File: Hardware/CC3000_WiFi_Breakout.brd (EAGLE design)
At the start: 40.6 x 35.6 mm, 33 parts, among them J1 U.FL, U1 V_REG_317SMD, U3 74HC4050, U5 CC3000

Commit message: Layout (mostly) done
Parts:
- U1: value V_REG_317SMD -> (none)
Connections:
- net 3.3V: now also U1.4
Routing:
- net 3.3V: track 101.9 -> 89.4 mm, vias 3 -> 13
- net VCC: track 45.2 -> 47.9 mm
- net D3: track 18.2 -> 16.6 mm
- added copper zone on layer 1, net 3.3V
- added copper zone on layer 16, net 3.3V

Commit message: Proto layout complete. Needs aesthetics.
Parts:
- moved LOGO2 48.2 mm to (27.7, 8.64), turned to 0 degrees
- moved AE1 30.7 mm to (10.2, 38.1), turned to 180 degrees
- moved J1 30.5 mm to (27.9, 36.8), turned to 270 degrees
- moved STANDOFF1 30.5 mm to (33.0, 33.0), turned to 90 degrees
- moved STANDOFF2 30.5 mm to (2.54, 33.0), turned to 90 degrees
- moved STANDOFF3 30.5 mm to (2.54, 2.54), turned to 90 degrees
- moved STANDOFF4 30.5 mm to (33.0, 2.54), turned to 90 degrees
- moved C7 28.7 mm to (17.8, 38.1), turned to 0 degrees
- moved L2 27.7 mm to (20.1, 37.2), turned to 270 degrees
- moved L1 27.7 mm to (15.5, 37.2), turned to 270 degrees
- moved JP2 27.1 mm to (27.9, 2.54), turned to 180 degrees
- moved C5 24.4 mm to (31.8, 7.62), turned to 180 degrees
- moved D1 21.7 mm to (3.81, 11.4), turned to 270 degrees
- moved C6 20.9 mm to (23.7, 31.3), turned to 270 degrees
- moved C1 20.5 mm to (8.89, 29.2), turned to 0 degrees
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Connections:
- net D4 renamed INT
- net D5 renamed CS
- removed net D1: JP2.1, U3.3
- removed net D2: JP2.2, U3.5
- removed net D3: JP2.3, U3.7
- new net EN: JP2.2, U3.3
- new net MOSI: JP2.7, U3.7
- new net SCK: JP2.3, U3.5
- net GND: now also JP2.1; no longer JP2.7
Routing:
- net D1: track 30.5 -> 0.00 mm, vias 2 -> 0
- net EN: track 0.00 -> 30.3 mm, vias 0 -> 2
- net D2: track 27.1 -> 0.00 mm, vias 1 -> 0
- net SCK: track 0.00 -> 23.4 mm, vias 0 -> 1
- net D3: track 16.6 -> 0.00 mm, vias 1 -> 0
- net MOSI: track 0.00 -> 6.95 mm
- net INT: track 10.0 -> 7.41 mm
- net VCC: track 47.9 -> 45.7 mm
- net CS: track 12.1 -> 10.1 mm
- net WIFI_EN: track 47.0 -> 48.7 mm
- net SPI_MISO: track 19.3 -> 18.0 mm
- net 3.3V: track 89.4 -> 88.4 mm
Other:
- board size 40.6 x 35.6 mm -> 35.6 x 40.6 mm

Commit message: Prototype board ready for review
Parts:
- U1: value (none) -> LM1117
- moved LOGO3 69.0 mm to (3.17, 26.7)
- moved LOGO1 61.2 mm to (3.81, 7.62)
- moved FID2 58.5 mm to (1.27, 6.35)
- moved FID1 38.6 mm to (34.3, 29.2)
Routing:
- net 3.3V: track 88.4 -> 88.9 mm
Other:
- board text added: "3.3V"
- board text added: "CS"
- board text added: "EN"
- board text added: "INT"
- board text added: "MISO"
- board text added: "MOSI"
- board text added: "SCK"
- board text added: "VCC"
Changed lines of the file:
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@@
 <setting verticaltext="up"/>
 </settings>
-<grid distance="0.05" unitdist="inch" unit="inch" style="dots" multiple="1" display="yes" altdistance="0.025" altunitdist="inch" altunit="inch"/>
+<grid distance="0.05" unitdist="inch" unit="inch" style="dots" multiple="1" display="yes" altdistance="0.005" altunitdist="inch" altunit="inch"/>
 <layers>
 <layer number="1" name="Top" color="4" fill="1" visible="yes" active="yes"/>
-<layer number="16" name="Bottom" color="1" fill="1" visible="no" active="yes"/>
+<layer number="16" name="Bottom" color="1" fill="1" visible="yes" active="yes"/>
 <layer number="17" name="Pads" color="2" fill="1" visible="yes" active="yes"/>
 <layer number="18" name="Vias" color="2" fill="1" visible="yes" active="yes"/>
@@
 <layer number="20" name="Dimension" color="15" fill="1" visible="yes" active="yes"/>
 <layer number="21" name="tPlace" color="16" fill="1" visible="yes" active="yes"/>
-<layer number="22" name="bPlace" color="14" fill="1" visible="no" active="yes"/>
+<layer number="22" name="bPlace" color="14" fill="1" visible="yes" active="yes"/>
 <layer number="23" name="tOrigins" color="15" fill="1" visible="yes" active="yes"/>
-<layer number="24" name="bOrigins" color="15" fill="1" visible="no" active="yes"/>
+<layer number="24" name="bOrigins" color="15" fill="1" visible="yes" active="yes"/>
 <layer number="25" name="tNames" color="7" fill="1" visible="no" active="yes"/>
 <layer number="26" name="bNames" color="7" fill="1" visible="no" active="yes"/>
@@
 <layer number="43" name="vRestrict" color="2" fill="10" visible="no" active="yes"/>
 <layer number="44" name="Drills" color="7" fill="1" visible="no" active="yes"/>
-<layer number="45" name="Holes" color="7" fill="1" visible="no" active="yes"/>
+<layer number="45" name="Holes" color="7" fill="1" visible="yes" active="yes"/>
 <layer number="46" name="Milling" color="3" fill="1" visible="no" active="yes"/>
-<layer number="51" name="tDocu" color="6" fill="1" visible="no" active="yes"/>
+<layer number="51" name="tDocu" color="6" fill="1" visible="yes" active="yes"/>
 <layer number="52" name="bDocu" color="7" fill="1" visible="no" active="yes"/>
 <layer number="33" name="tFinish" color="6" fill="3" visible="no" active="no"/>
@@
 <text x="15.875" y="24.13" size="0.8128" layer="21" font="vector" ratio="15" rot="R90" align="center">RX</text>
 <text x="15.875" y="26.67" size="0.8128" layer="21" font="vector" ratio="15" rot="R270" align="center">TX</text>
-<text x="95.25" y="3.175" size="1.016" layer="21" font="vector" ratio="15" rot="R270" align="center">Debug</text>
+<text x="17.78" y="28.575" size="0.8128" layer="21" font="vector" ratio="15" rot="R180" align="center">Debug</text>
 <text x="31.75" y="-16.51" size="1.778" layer="25" font="vector">Shawn Hymel</text>
 <text x="34.29" y="20.32" size="1.2192" layer="16" font="vector" ratio="15" rot="MR270" align="center">v01</text>
-<text x="85.09" y="10.16" size="1.397" layer="21" font="vector" ratio="15" rot="R180" align="bottom-center">CC3000</text>
-<text x="85.09" y="15.24" size="1.397" layer="21" font="vector" ratio="15" align="bottom-center">WiFi Breakout</text>
-<text x="74.93" y="30.48" size="1.016" layer="21" font="vector" ratio="15" align="bottom-center">802.11b/g</text>
-<text x="76.2" y="2.54" size="1.016" layer="21" font="vector" ratio="15" rot="R90" align="bottom-center">PWR</text>
+<text x="15.24" y="32.0548" size="1.27" layer="21" font="vector" ratio="15" align="bottom-center">CC3000</text>
+<text x="15.24" y="30.5816" size="1.27" layer="21" font="vector" ratio="15" align="bottom-center">WiFi Breakout</text>
+<text x="26.67" y="9.144" size="1.016" layer="21" font="vector" ratio="15" align="bottom-center">802.11b/g</text>
+<text x="1.27" y="11.43" size="0.8128" layer="21" font="vector" ratio="15" rot="R270" align="bottom-center">PWR</text>
 <wire x1="0" y1="40.64" x2="0" y2="0" width="0.2032" layer="20"/>
 <wire x1="0" y1="0" x2="35.56" y2="0" width="0.2032" layer="20"/>
@@
 <vertex x="0" y="37.846"/>
 </polygon>
+<text x="27.94" y="0.7112" size="0.8128" layer="21" font="vector" ratio="15" align="center">GND</text>
+<text x="25.4" y="4.3688" size="0.8128" layer="21" font="vector" ratio="15" align="center">EN</text>
+<text x="22.86" y="0.7112" size="0.8128" layer="21" font="vector" ratio="15" align="center">SCK</text>
+<text x="20.32" y="4.3688" size="0.8128" layer="21" font="vector" ratio="15" align="center">INT</text>
+<text x="17.78" y="0.7112" size="0.8128" layer="21" font="vector" ratio="15" align="center">CS</text>
+<text x="15.24" y="4.3688" size="0.8128" layer="21" font="vector" ratio="15" align="center">MISO</text>
+<text x="12.7" y="0.7112" size="0.8128" layer="21" font="vector" ratio="15" align="center">MOSI</text>
+<text x="10.16" y="4.3688" size="0.8128" layer="21" font="vector" ratio="15" align="center">3.3V</text>
+<text x="7.62" y="0.7112" size="0.8128" layer="21" font="vector" ratio="15" align="center">VCC</text>
 </plain>
 <attributes>
@@
 <param name="dpGapFactor" value="2.5"/>
 <param name="checkGrid" value="0"/>
-<param name="checkAngle" value="1"/>
+<param name="checkAngle" value="0"/>
 <param name="checkFont" value="1"/>
 <param name="checkRestrict" value="1"/>
@@
 <element name="R1" library="SparkFun-Resistors" package="0603-RES" value="240" x="8.89" y="17.78" rot="R180"/>
 <element name="R2" library="SparkFun-Resistors" package="0603-RES" value="390" x="13.97" y="17.78" rot="R180"/>
-<element name="U1" library="SparkFun-PowerIC" package="SOT223" value="" x="6.35" y="22.86" rot="R90"/>
+<element name="U1" library="SparkFun-PowerIC" package="SOT223" value="LM1117" x="6.35" y="22.86" rot="R90"/>
 <element name="U3" library="SparkFun-DigitalIC" package="SO016" value="74HC4050" x="11.43" y="10.16" rot="R270"/>
 <element name="SJ1" library="SparkFun-Passives" package="SJ_3_PASTE1&amp;2" value="Mode" x="17.78" y="11.43" rot="R180"/>
@@
 </element>
 <element name="R4" library="SparkFun-Resistors" package="0603-RES" value="10k" x="3.81" y="17.78" rot="R180"/>
-<element name="FID1" library="SparkFun-Aesthetics" package="FIDUCIAL-1X2" value="FIDUCIAL1X2" x="62.23" y="2.54"/>
-<element name="FID2" library="SparkFun-Aesthetics" package="FIDUCIAL-1X2" value="FIDUCIAL1X2" x="59.69" y="2.54"/>
-<element name="LOGO1" library="SparkFun-Aesthetics" package="OSHW-LOGO-S" value="OSHW-LOGOS" x="64.77" y="2.54"/>
+<element name="FID1" library="SparkFun-Aesthetics" package="FIDUCIAL-1X2" value="FIDUCIAL1X2" x="34.29" y="29.21"/>
+<element name="FID2" library="SparkFun-Aesthetics" package="FIDUCIAL-1X2" value="FIDUCIAL1X2" x="1.27" y="6.35"/>
+<element name="LOGO1" library="SparkFun-Aesthetics" package="OSHW-LOGO-S" value="OSHW-LOGOS" x="3.81" y="7.62"/>
 <element name="LOGO2" library="SparkFun-Aesthetics" package="SFE-NEW-WEBLOGO" value="LOGO-SFENEW" x="27.686" y="8.636" rot="MR0"/>
-<element name="LOGO3" library="SparkFun-Aesthetics" package="SFE-LOGO-FLAME" value="LOGO-SFESK" x="67.31" y="1.27"/>
+<element name="LOGO3" library="SparkFun-Aesthetics" package="SFE-LOGO-FLAME" value="LOGO-SFESK" x="3.175" y="26.67"/>
 <element name="JP2" library="SparkFun-Connectors" package="1X09" value="M09" x="27.94" y="2.54" rot="R180"/>
 <element name="STANDOFF1" library="SparkFun-Electromechanical" package="STAND-OFF" value="STAND-OFF" x="33.02" y="33.02" rot="R90"/>
@@
 <wire x1="2.96" y1="17.78" x2="2.96" y2="17.106" width="0.254" layer="1"/>
 <wire x1="2.96" y1="17.106" x2="3.81" y2="16.256" width="0.254" layer="1"/>
-<wire x1="3.81" y1="16.256" x2="5.334" y2="16.256" width="0.254" layer="1"/>
-<wire x1="5.334" y1="16.256" x2="6.731" y2="14.859" width="0.254" layer="1"/>
-<wire x1="6.731" y1="14.859" x2="6.985" y2="14.605" width="0.254" layer="1"/>
-<wire x1="8.63" y1="14.605" x2="6.985" y2="14.605" width="0.254" layer="1"/>
-<wire x1="4.66" y1="13.97" x2="5.842" y2="13.97" width="0.254" layer="1"/>
-<wire x1="5.842" y1="13.97" x2="6.731" y2="14.859" width="0.254" layer="1"/>
+<wire x1="3.81" y1="16.256" x2="5.842" y2="16.256" width="0.254" layer="1"/>
+<wire x1="4.66" y1="13.97" x2="6.35" y2="13.97" width="0.254" layer="1"/>
 <contactref element="U1" pad="4"/>
 <polygon width="0.254" layer="1" isolate="0.3048">
@@
 <wire x1="29.464" y1="8.128" x2="27.178" y2="10.414" width="0.508" layer="16"/>
 <wire x1="27.178" y1="10.414" x2="21.336" y2="10.414" width="0.508" layer="16"/>
-</signal>
-<signal name="GND" airwireshidden="yes">
+<wire x1="8.63" y1="14.605" x2="7.493" y2="14.605" width="0.254" layer="1"/>
+<wire x1="7.493" y1="14.605" x2="7.239" y2="14.859" width="0.254" layer="1"/>
+<wire x1="7.239" y1="14.859" x2="5.842" y2="16.256" width="0.254" layer="1"/>
+<wire x1="6.35" y1="13.97" x2="7.239" y2="14.859" width="0.254" layer="1"/>
+</signal>
+<signal name="GND">
 <contactref element="C1" pad="C"/>
 <contactref element="C3" pad="2"/>
@@
 <via x="20.828" y="27.94" extent="1-16" drill="0.381"/>
 <via x="19.431" y="14.859" extent="1-16" drill="0.381"/>
+<via x="13.97" y="15.748" extent="1-16" drill="0.508"/>
+<via x="1.016" y="28.956" extent="1-16" drill="0.508"/>
+<via x="16.51" y="29.845" extent="1-16" drill="0.508"/>
+<via x="5.1308" y="15.2908" extent="1-16" drill="0.508"/>
+<via x="5.842" y="1.016" extent="1-16" drill="0.508"/>
+<via x="29.718" y="1.016" extent="1-16" drill="0.508"/>
+<via x="34.036" y="6.096" extent="1-16" drill="0.508"/>
+<via x="11.43" y="8.128" extent="1-16" drill="0.508"/>
+<via x="6.604" y="32.004" extent="1-16" drill="0.508"/>
+<via x="23.876" y="4.572" extent="1-16" drill="0.508"/>
+<via x="21.844" y="4.572" extent="1-16" drill="0.508"/>
+<via x="34.29" y="39.37" extent="1-16" drill="0.508"/>
 </signal>
 <signal name="WIFI_CS">
@@
 <wire x1="15.748" y1="4.572" x2="13.462" y2="4.572" width="0.254" layer="1"/>
 </signal>
+<signal name="N$1">
+<via x="16.002" y="25.4" extent="1-16" drill="0.508"/>
+</signal>
 </signals>

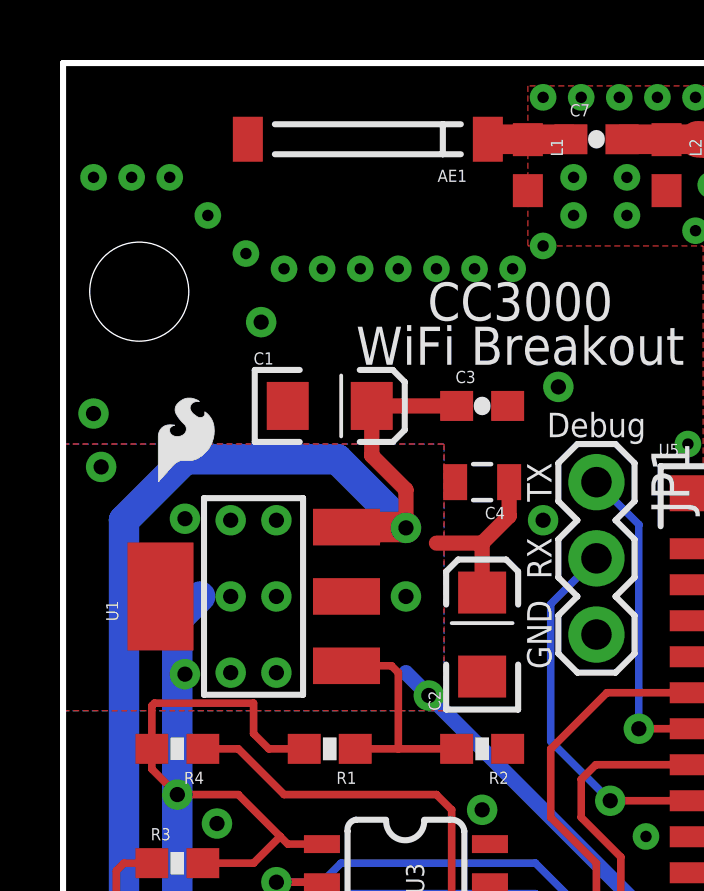
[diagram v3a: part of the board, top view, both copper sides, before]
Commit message: Ready for prototype
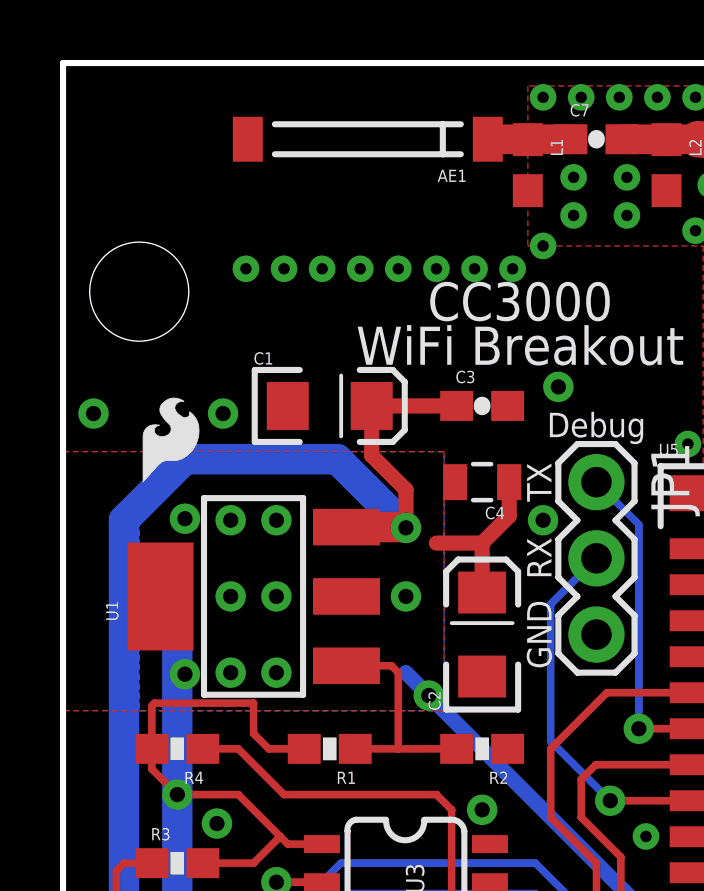
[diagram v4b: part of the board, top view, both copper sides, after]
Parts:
- moved LOGO3 0.51 mm to (2.67, 26.7)
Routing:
- net 3.3V: track 88.9 -> 87.8 mm, vias 13 -> 12
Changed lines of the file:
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@@
 <setting verticaltext="up"/>
 </settings>
-<grid distance="0.05" unitdist="inch" unit="inch" style="dots" multiple="1" display="yes" altdistance="0.005" altunitdist="inch" altunit="inch"/>
+<grid distance="0.1" unitdist="inch" unit="inch" style="dots" multiple="1" display="yes" altdistance="0.05" altunitdist="inch" altunit="inch"/>
 <layers>
 <layer number="1" name="Top" color="4" fill="1" visible="yes" active="yes"/>
@@
 <vertex x="14.986" y="40.64"/>
 <vertex x="14.986" y="34.798"/>
-<vertex x="6.858" y="34.798"/>
-<vertex x="3.81" y="37.846"/>
-<vertex x="0" y="37.846"/>
+<vertex x="0" y="34.798"/>
 <vertex x="0" y="40.64"/>
 </polygon>
@@
 <vertex x="14.986" y="40.64"/>
 <vertex x="14.986" y="34.798"/>
-<vertex x="6.858" y="34.798"/>
-<vertex x="3.81" y="37.846"/>
-<vertex x="0" y="37.846"/>
+<vertex x="0" y="34.798"/>
 </polygon>
 <text x="27.94" y="0.7112" size="0.8128" layer="21" font="vector" ratio="15" align="center">GND</text>
@@
 <text x="10.16" y="4.3688" size="0.8128" layer="21" font="vector" ratio="15" align="center">3.3V</text>
 <text x="7.62" y="0.7112" size="0.8128" layer="21" font="vector" ratio="15" align="center">VCC</text>
+<text x="15.24" y="32.0548" size="1.27" layer="22" font="vector" ratio="15" rot="MR0" align="bottom-center">CC3000</text>
+<text x="14.986" y="30.5816" size="1.27" layer="22" font="vector" ratio="15" rot="MR0" align="bottom-center">WiFi Breakout</text>
+<text x="7.62" y="0.7112" size="0.8128" layer="22" font="vector" ratio="15" rot="MR0" align="center">VCC</text>
+<text x="10.16" y="4.3688" size="0.8128" layer="22" font="vector" ratio="15" rot="MR0" align="center">3.3V</text>
+<text x="12.7" y="0.7112" size="0.8128" layer="22" font="vector" ratio="15" rot="MR0" align="center">MOSI</text>
+<text x="15.24" y="4.3688" size="0.8128" layer="22" font="vector" ratio="15" rot="MR0" align="center">MISO</text>
+<text x="17.78" y="0.7112" size="0.8128" layer="22" font="vector" ratio="15" rot="MR0" align="center">CS</text>
+<text x="20.32" y="4.3688" size="0.8128" layer="22" font="vector" ratio="15" rot="MR0" align="center">INT</text>
+<text x="22.86" y="0.7112" size="0.8128" layer="22" font="vector" ratio="15" rot="MR0" align="center">SCK</text>
+<text x="25.4" y="4.3688" size="0.8128" layer="22" font="vector" ratio="15" rot="MR0" align="center">EN</text>
+<text x="27.94" y="0.7112" size="0.8128" layer="22" font="vector" ratio="15" rot="MR0" align="center">GND</text>
 </plain>
 <attributes>
@@
 <element name="LOGO1" library="SparkFun-Aesthetics" package="OSHW-LOGO-S" value="OSHW-LOGOS" x="3.81" y="7.62"/>
 <element name="LOGO2" library="SparkFun-Aesthetics" package="SFE-NEW-WEBLOGO" value="LOGO-SFENEW" x="27.686" y="8.636" rot="MR0"/>
-<element name="LOGO3" library="SparkFun-Aesthetics" package="SFE-LOGO-FLAME" value="LOGO-SFESK" x="3.175" y="26.67"/>
+<element name="LOGO3" library="SparkFun-Aesthetics" package="SFE-LOGO-FLAME" value="LOGO-SFESK" x="2.667" y="26.67"/>
 <element name="JP2" library="SparkFun-Connectors" package="1X09" value="M09" x="27.94" y="2.54" rot="R180"/>
 <element name="STANDOFF1" library="SparkFun-Electromechanical" package="STAND-OFF" value="STAND-OFF" x="33.02" y="33.02" rot="R90"/>
@@
 <wire x1="3.81" y1="8.89" x2="3.81" y2="16.256" width="1.016" layer="16"/>
 <wire x1="3.81" y1="16.256" x2="3.81" y2="22.098" width="1.016" layer="16"/>
-<wire x1="3.81" y1="22.098" x2="4.572" y2="22.86" width="1.016" layer="16"/>
 <via x="3.81" y="16.256" extent="1-16" drill="0.508"/>
 <wire x1="13.97" y1="22.99" x2="13.97" y2="24.638" width="0.508" layer="1"/>
@@
 <polygon width="0.254" layer="1" isolate="0.3048">
 <vertex x="0" y="19.05"/>
-<vertex x="0" y="27.94"/>
-<vertex x="12.7" y="27.94"/>
+<vertex x="0" y="27.686"/>
+<vertex x="12.7" y="27.686"/>
 <vertex x="12.7" y="19.05"/>
 </polygon>
@@
 <wire x1="13.97" y1="24.638" x2="12.446" y2="24.638" width="0.508" layer="1"/>
 <polygon width="0.254" layer="16" isolate="0.3048">
-<vertex x="0" y="19.05"/>
+<vertex x="2.54" y="19.05"/>
 <vertex x="12.7" y="19.05"/>
-<vertex x="12.7" y="27.94"/>
-<vertex x="0" y="27.94"/>
+<vertex x="12.7" y="27.686"/>
+<vertex x="4.191" y="27.686"/>
+<vertex x="2.54" y="26.035"/>
 </polygon>
 <via x="12.192" y="19.558" extent="1-16" drill="0.508"/>
 <via x="4.064" y="25.4508" extent="1-16" drill="0.508"/>
 <via x="4.064" y="20.2692" extent="1-16" drill="0.508"/>
-<via x="1.27" y="27.178" extent="1-16" drill="0.508"/>
 <via x="5.588" y="20.32" extent="1-16" drill="0.508"/>
 <via x="7.112" y="20.32" extent="1-16" drill="0.508"/>
@@
 <via x="29.337" y="32.639" extent="1-16" drill="0.381"/>
 <via x="29.337" y="33.909" extent="1-16" drill="0.381"/>
-<via x="6.096" y="34.29" extent="1-16" drill="0.381"/>
-<via x="4.826" y="35.56" extent="1-16" drill="0.381"/>
-<via x="3.556" y="36.83" extent="1-16" drill="0.381"/>
-<via x="2.286" y="36.83" extent="1-16" drill="0.381"/>
-<via x="1.016" y="36.83" extent="1-16" drill="0.381"/>
+<via x="6.096" y="33.782" extent="1-16" drill="0.381"/>
 <via x="16.002" y="34.544" extent="1-16" drill="0.381"/>
 <polygon width="0.254" layer="1" isolate="0.3048" rank="6">
@@
 <via x="34.036" y="6.096" extent="1-16" drill="0.508"/>
 <via x="11.43" y="8.128" extent="1-16" drill="0.508"/>
-<via x="6.604" y="32.004" extent="1-16" drill="0.508"/>
+<via x="5.334" y="28.956" extent="1-16" drill="0.508"/>
 <via x="23.876" y="4.572" extent="1-16" drill="0.508"/>
 <via x="21.844" y="4.572" extent="1-16" drill="0.508"/>
